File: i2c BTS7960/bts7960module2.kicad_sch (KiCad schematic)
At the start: 43 parts, among them J3 jst, J4 Conn_01x04, J9 Conn_01x02, U1 74AHC244, U2 BTS7960B, U3 BTS7960B, U4 BTS7960B, U6 BTS7960B

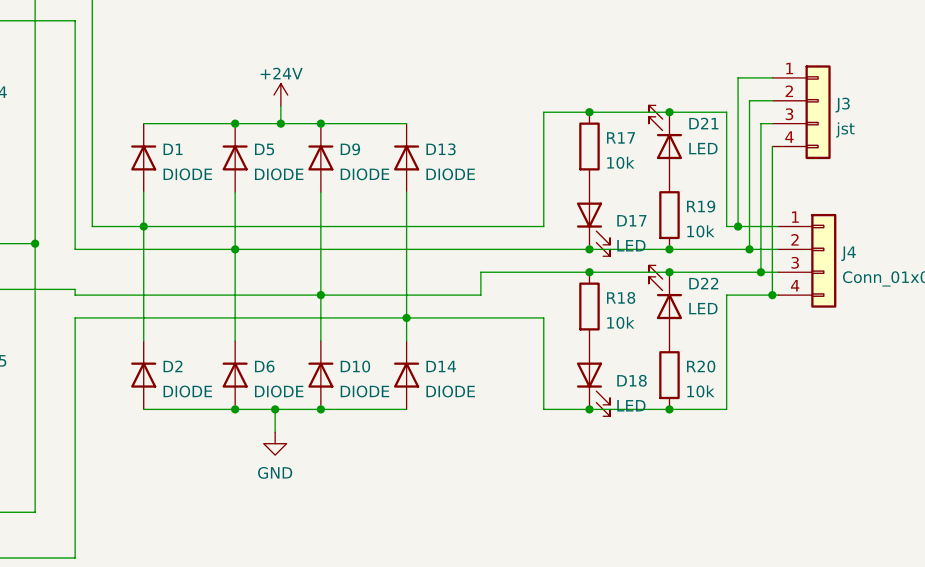
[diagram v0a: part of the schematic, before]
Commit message: motor controller DFM
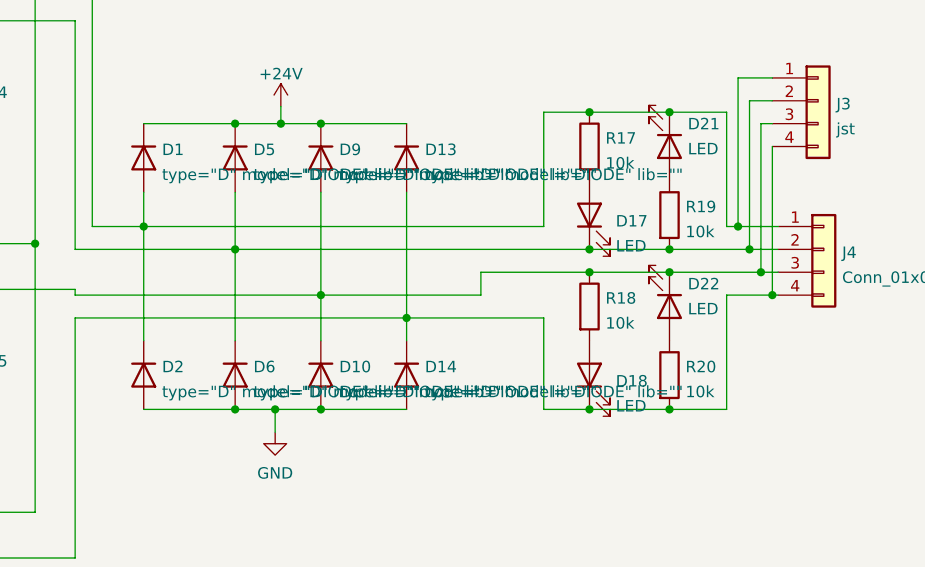
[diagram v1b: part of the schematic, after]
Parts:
- D1, D10, D13, D14, D2, D5, D6, D9: value DIODE -> ${SIM.PARAMS}; Spice_Netlist_Enabled Y -> (none); Spice_Primitive D -> (none)
